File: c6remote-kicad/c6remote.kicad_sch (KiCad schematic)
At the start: 27 parts, among them J1 Battery, Q1 MMBT2222A, SW1 SW_Push, SW10 SW_Push, SW11 SW_Push, SW2 SW_Push, SW3 SW_Push, SW4 SW_Push, SW5 SW_Push, SW6 SW_Push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

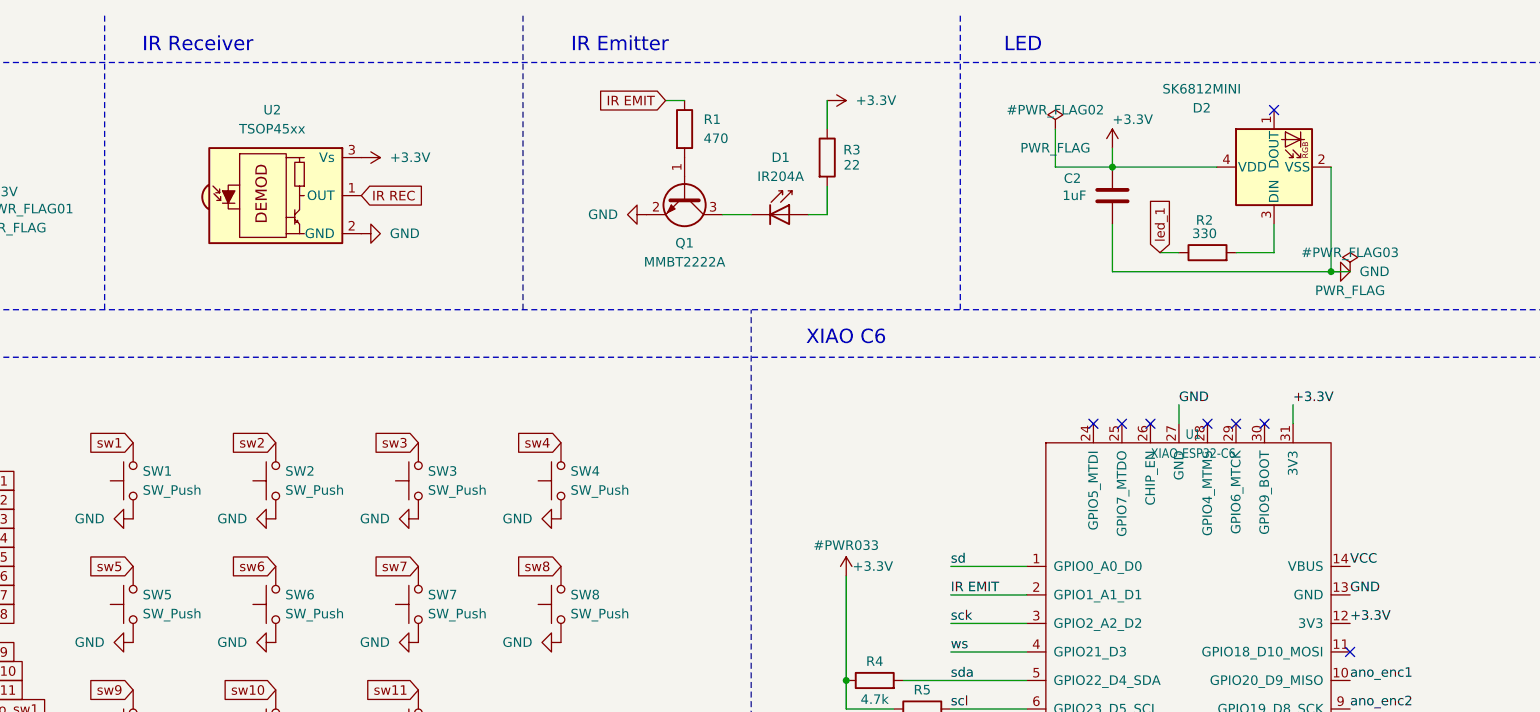
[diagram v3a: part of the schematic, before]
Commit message: feat(schematic): add TSOP U2 supply filter R6 100Ω inline + C3 100nF bypass; relocate PWR_FLAG02 onto filtered Vs net (resistor breaks power chain for ERC); convert VCC local label to global so net stays 'VCC' on PCB sync (no /VCC); ERC 0 errors, DRC 0 errors
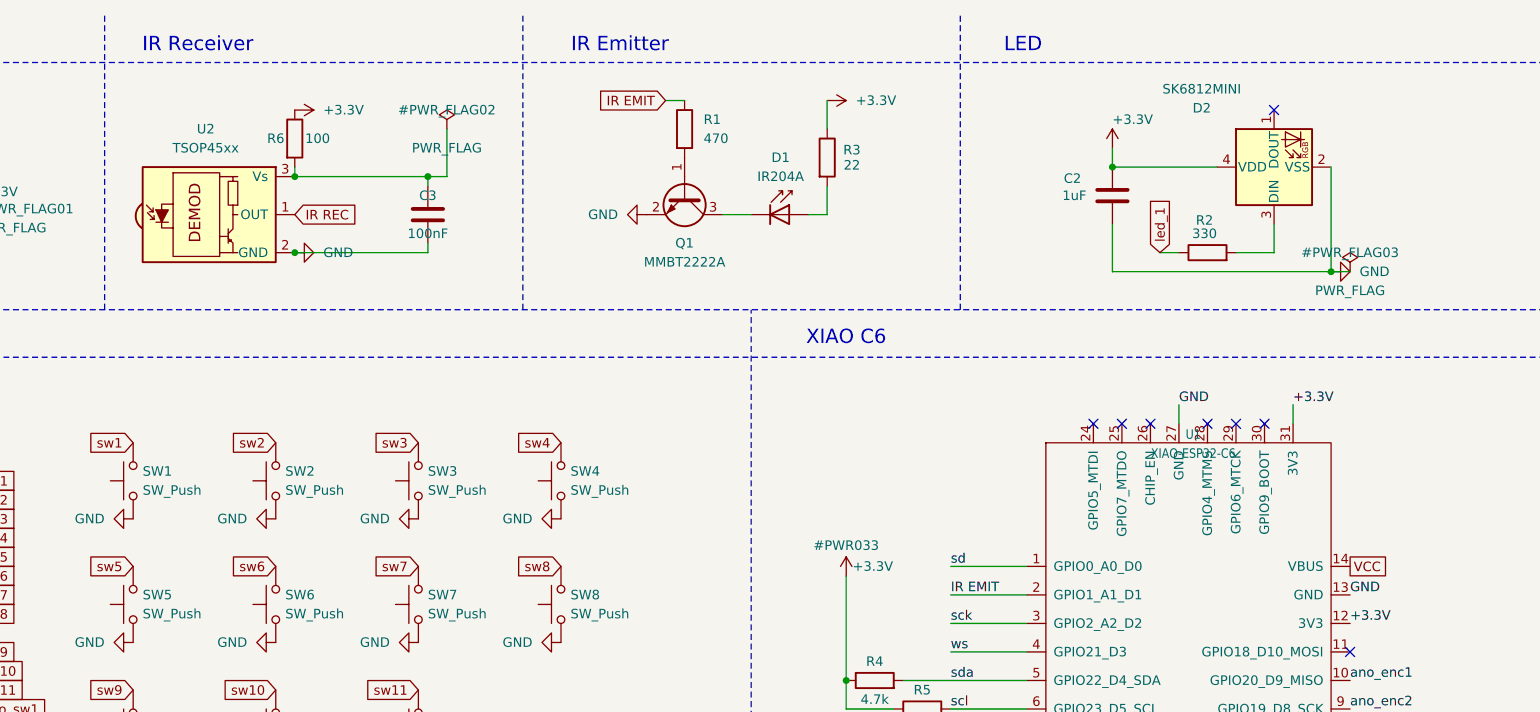
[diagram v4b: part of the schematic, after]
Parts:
- added C3: 100nF, Capacitor_SMD:C_0603_1608Metric, symbol Device:C
- added R6: 100, Resistor_SMD:R_0603_1608Metric, symbol Device:R
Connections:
- net +3.3V: now also R6.1; no longer U2.3 (Vs)
- net GND: now also C3.2
- new net: C3.1, R6.2, U2.3 (Vs)
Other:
- moved on the sheet: U2
